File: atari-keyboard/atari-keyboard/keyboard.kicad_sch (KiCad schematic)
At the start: 210 parts, among them SW201 MENU, SW202 TURBO, SW203 RESET, SW204 OPTION, SW205 SELECT, SW206 START, SW207 HELP, SW208 ESC, SW209 RSHIFT, SW210 1, SW211 2, SW212 3, SW213 4, SW214 5, SW215 6, SW216 7, SW217 8, SW218 UP, SW219 9, SW220 0, SW221 <, SW222 >, SW223 BS, SW224 BRK, SW225 TAB, SW226 Q, SW227 DOWN, SW228 W, SW229 E, SW230 R, SW231 T, SW232 Y, SW233 U, SW234 I, SW235 O, SW236 LEFT, SW237 P, SW238 [-], SW239 [=], SW240 RET, SW241 CTRL, SW242 A, SW243 S, SW244 D, SW245 RIGHT, SW246 F, SW247 G, SW248 H, SW249 J, SW250 K, SW251 L, SW252 [;], SW253 [+], SW254 N, SW255 MULT, SW256 CAPS, SW257 LSHIFT, SW258 Z, SW259 X, SW260 C, SW261 V, SW262 B, SW263 M, SW264 FN, SW265 INV, SW266 SPC, SW267 [,], SW268 [.], SW269 [/], SW270 POWER

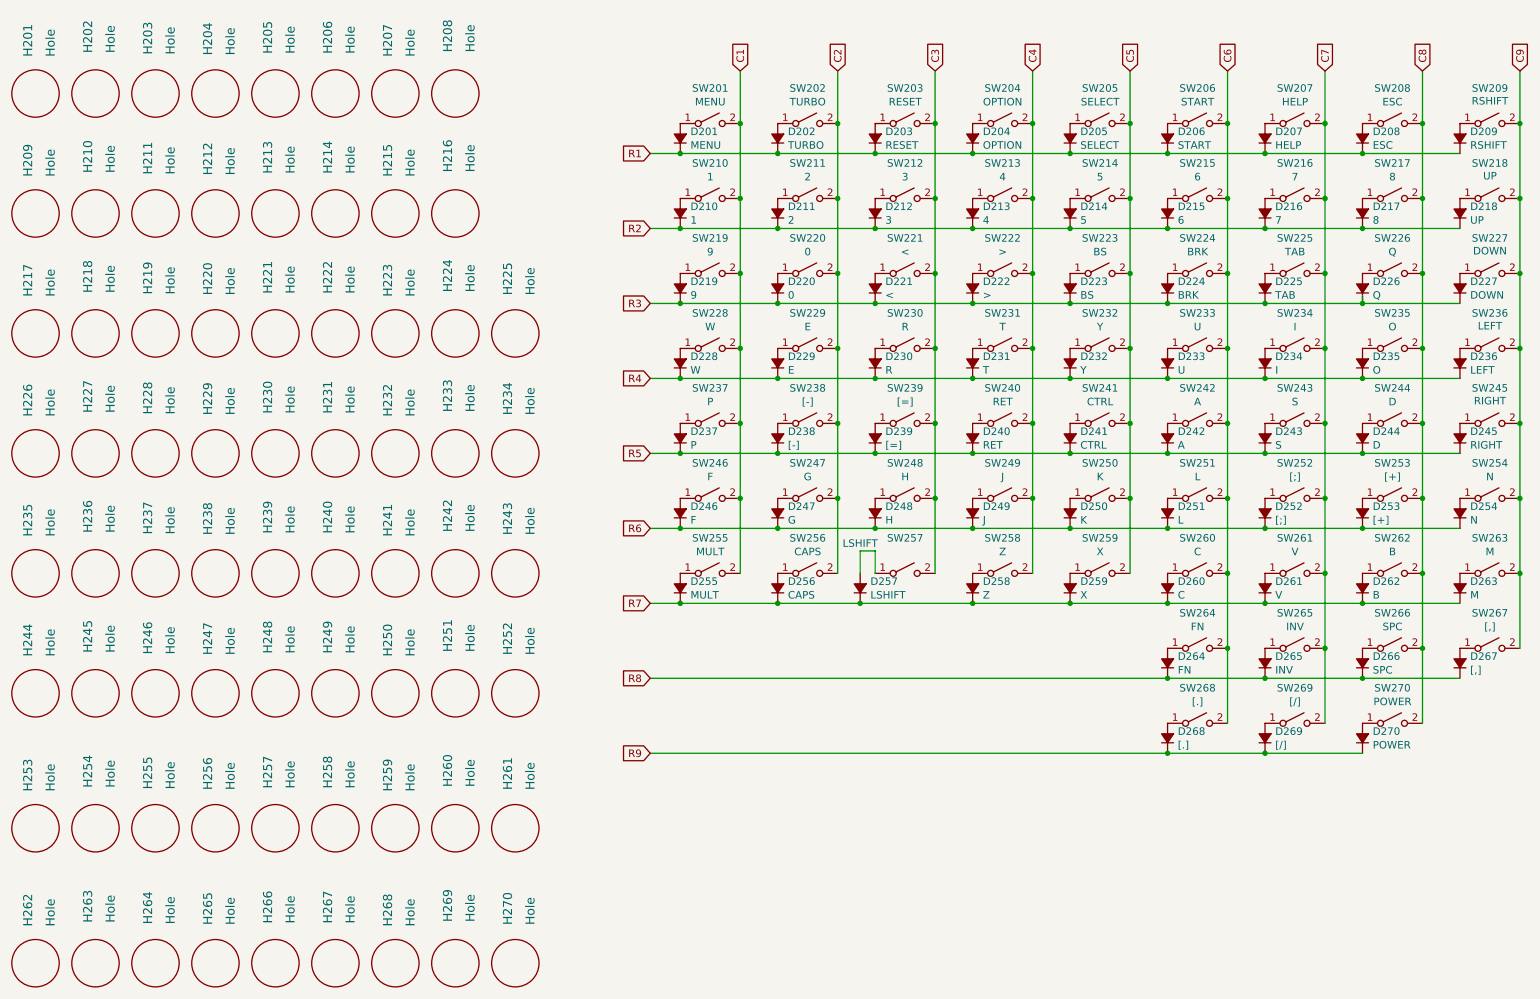
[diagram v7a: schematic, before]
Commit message: Better autogen openscad layout.  generated jlc bom&cpl
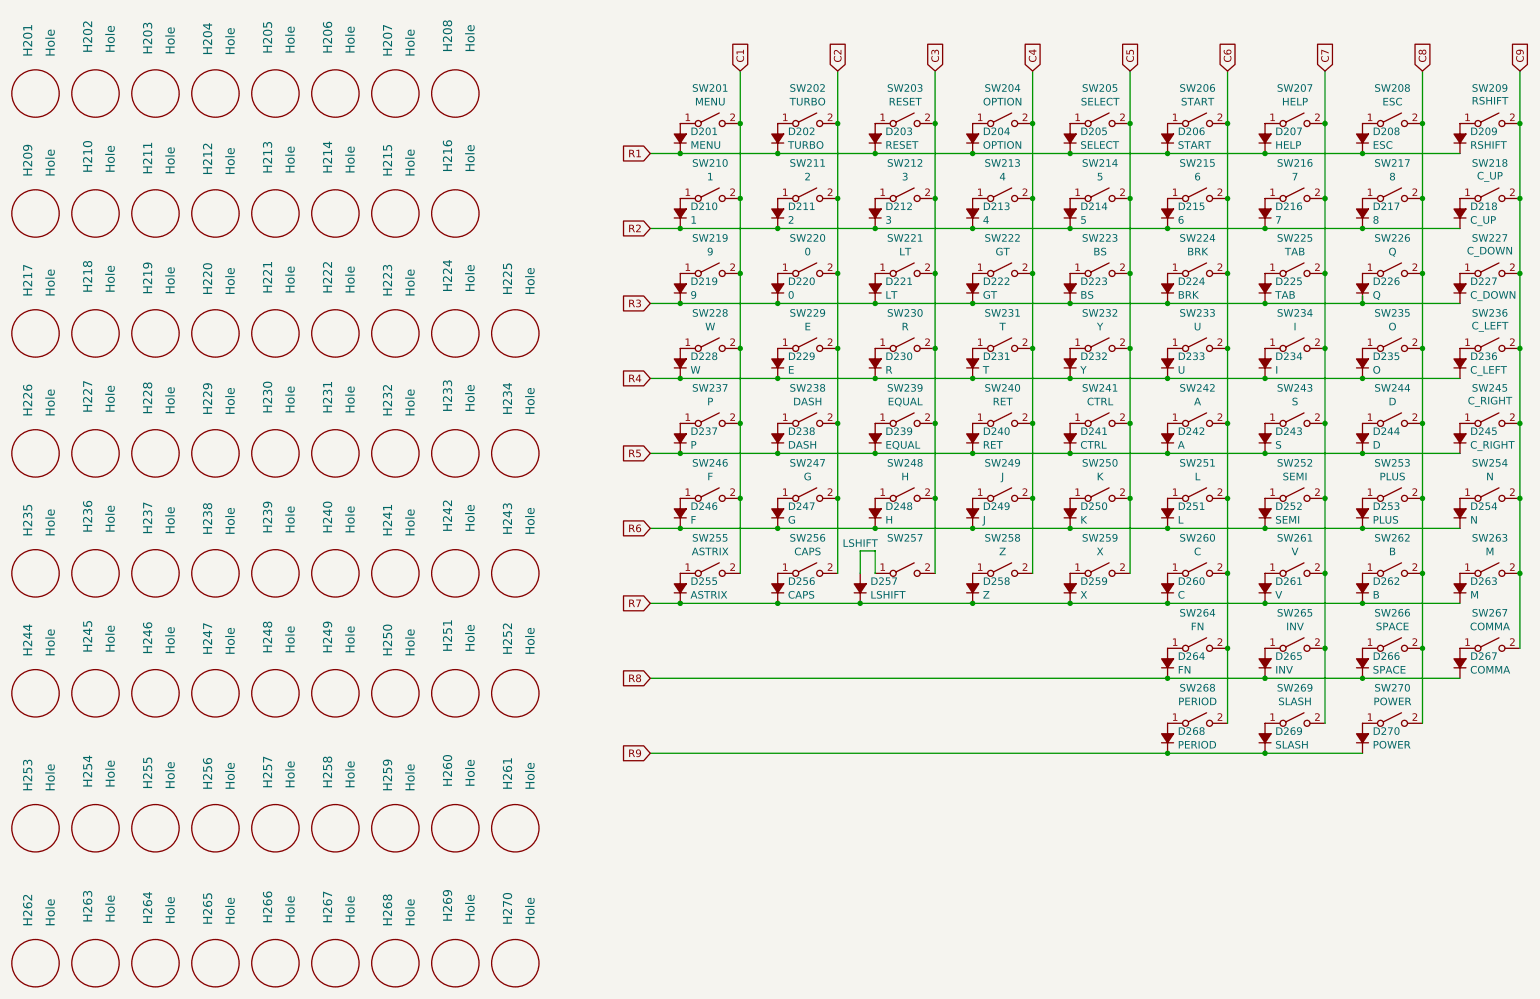
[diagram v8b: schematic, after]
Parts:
- D218, SW218: value UP -> C_UP
- D221, SW221: value < -> LT
- D222, SW222: value > -> GT
- D227, SW227: value DOWN -> C_DOWN
- D236, SW236: value LEFT -> C_LEFT
- D238, SW238: value [-] -> DASH
- D239, SW239: value [=] -> EQUAL
- D245, SW245: value RIGHT -> C_RIGHT
- D252, SW252: value [;] -> SEMI
- D253, SW253: value [+] -> PLUS
- D255, SW255: value MULT -> ASTRIX
- D266, SW266: value SPC -> SPACE
- D267, SW267: value [,] -> COMMA
- D268, SW268: value [.] -> PERIOD
- D269, SW269: value [/] -> SLASH
- H240: PCB_X 2 -> 4
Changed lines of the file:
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@@
       (effects (font (size 1.27 1.27)) (justify right))
     )
-    (property "Value" "[;]" (id 1) (at 237.9472 110.363 90)
+    (property "Value" "SEMI" (id 1) (at 237.9472 110.363 90)
       (effects (font (size 1.27 1.27)) (justify right))
     )
@@
     (in_bom yes) (on_board yes)
     (property "Reference" "SW253" (id 0) (at 257.81 100.711 0))
-    (property "Value" "[+]" (id 1) (at 257.81 103.0224 0))
+    (property "Value" "PLUS" (id 1) (at 257.81 103.0224 0))
     (property "Footprint" "Button_Switch_Keyboard:SW_Cherry_MX_1.00u_PCB" (id 2) (at 257.81 106.68 0)
       (effects (font (size 1.27 1.27)) hide)
@@
     (in_bom yes) (on_board yes)
     (property "Reference" "SW266" (id 0) (at 257.81 126.111 0))
-    (property "Value" "SPC" (id 1) (at 257.81 128.4224 0))
+    (property "Value" "SPACE" (id 1) (at 257.81 128.4224 0))
     (property "Footprint" "Button_Switch_Keyboard:SW_Cherry_MX_6.25u_PCB" (id 2) (at 257.81 132.08 0)
       (effects (font (size 1.27 1.27)) hide)
@@
     (in_bom yes) (on_board yes)
     (property "Reference" "SW238" (id 0) (at 158.75 88.011 0))
-    (property "Value" "[-]" (id 1) (at 158.75 90.3224 0))
+    (property "Value" "DASH" (id 1) (at 158.75 90.3224 0))
     (property "Footprint" "Button_Switch_Keyboard:SW_Cherry_MX_1.00u_PCB" (id 2) (at 158.75 93.98 0)
       (effects (font (size 1.27 1.27)) hide)
@@
       (effects (font (size 1.27 1.27)) (justify right))
     )
-    (property "Value" "RIGHT" (id 1) (at 270.9672 97.663 90)
+    (property "Value" "C_RIGHT" (id 1) (at 270.9672 97.663 90)
       (effects (font (size 1.27 1.27)) (justify right))
     )
@@
       (effects (font (size 1.27 1.27)) (justify right))
     )
-    (property "Value" "[/]" (id 1) (at 237.9472 148.463 90)
+    (property "Value" "SLASH" (id 1) (at 237.9472 148.463 90)
       (effects (font (size 1.27 1.27)) (justify right))
     )
@@
       (effects (font (size 1.27 1.27)) (justify right))
     )
-    (property "Value" "[=]" (id 1) (at 171.9072 97.663 90)
+    (property "Value" "EQUAL" (id 1) (at 171.9072 97.663 90)
       (effects (font (size 1.27 1.27)) (justify right))
     )
@@
       (effects (font (size 1.27 1.27)) (justify right))
     )
-    (property "Value" "MULT" (id 1) (at 138.8872 123.063 90)
+    (property "Value" "ASTRIX" (id 1) (at 138.8872 123.063 90)
       (effects (font (size 1.27 1.27)) (justify right))
     )
@@
       (effects (font (size 1.27 1.27)) (justify right))
     )
-    (property "Value" "[,]" (id 1) (at 270.9672 135.763 90)
+    (property "Value" "COMMA" (id 1) (at 270.9672 135.763 90)
       (effects (font (size 1.27 1.27)) (justify right))
     )
@@
     (in_bom yes) (on_board yes)
     (property "Reference" "SW227" (id 0) (at 274.32 62.611 0))
-    (property "Value" "DOWN" (id 1) (at 274.32 64.77 0))
+    (property "Value" "C_DOWN" (id 1) (at 274.32 64.77 0))
     (property "Footprint" "Button_Switch_Keyboard:SW_Cherry_MX_1.00u_PCB" (id 2) (at 274.32 68.58 0)
       (effects (font (size 1.27 1.27)) hide)
@@
     (in_bom yes) (on_board yes)
     (property "Reference" "SW218" (id 0) (at 274.32 49.911 0))
-    (property "Value" "UP" (id 1) (at 274.32 52.07 0))
+    (property "Value" "C_UP" (id 1) (at 274.32 52.07 0))
     (property "Footprint" "Button_Switch_Keyboard:SW_Cherry_MX_1.00u_PCB" (id 2) (at 274.32 55.88 0)
       (effects (font (size 1.27 1.27)) hide)
@@
       (effects (font (size 1.27 1.27)) (justify right))
     )
-    (property "Value" "SPC" (id 1) (at 254.4572 135.763 90)
+    (property "Value" "SPACE" (id 1) (at 254.4572 135.763 90)
       (effects (font (size 1.27 1.27)) (justify right))
     )
@@
       (effects (font (size 1.27 1.27)) (justify right))
     )
-    (property "Value" "[.]" (id 1) (at 221.4372 148.463 90)
+    (property "Value" "PERIOD" (id 1) (at 221.4372 148.463 90)
       (effects (font (size 1.27 1.27)) (justify right))
     )
@@
       (effects (font (size 1.27 1.27)) (justify right))
     )
-    (property "Value" "DOWN" (id 1) (at 270.9672 72.263 90)
+    (property "Value" "C_DOWN" (id 1) (at 270.9672 72.263 90)
       (effects (font (size 1.27 1.27)) (justify right))
     )
@@
     (in_bom yes) (on_board yes)
     (property "Reference" "SW236" (id 0) (at 274.32 75.311 0))
-    (property "Value" "LEFT" (id 1) (at 274.32 77.47 0))
+    (property "Value" "C_LEFT" (id 1) (at 274.32 77.47 0))
     (property "Footprint" "Button_Switch_Keyboard:SW_Cherry_MX_1.00u_PCB" (id 2) (at 274.32 81.28 0)
       (effects (font (size 1.27 1.27)) hide)
@@
       (effects (font (size 1.27 1.27)) (justify right))
     )
-    (property "Value" "UP" (id 1) (at 270.9672 59.563 90)
+    (property "Value" "C_UP" (id 1) (at 270.9672 59.563 90)
       (effects (font (size 1.27 1.27)) (justify right))
     )
@@
       (effects (font (size 1.27 1.27)) (justify right))
     )
-    (property "Value" "[+]" (id 1) (at 254.4572 110.363 90)
+    (property "Value" "PLUS" (id 1) (at 254.4572 110.363 90)
       (effects (font (size 1.27 1.27)) (justify right))
     )
@@
     (in_bom yes) (on_board yes)
     (property "Reference" "SW268" (id 0) (at 224.79 138.811 0))
-    (property "Value" "[.]" (id 1) (at 224.79 141.1224 0))
+    (property "Value" "PERIOD" (id 1) (at 224.79 141.1224 0))
     (property "Footprint" "Button_Switch_Keyboard:SW_Cherry_MX_1.00u_PCB" (id 2) (at 224.79 144.78 0)
       (effects (font (size 1.27 1.27)) hide)
@@
       (effects (font (size 1.27 1.27)) (justify right))
     )
-    (property "Value" "<" (id 1) (at 171.9072 72.263 90)
+    (property "Value" "LT" (id 1) (at 171.9072 72.263 90)
       (effects (font (size 1.27 1.27)) (justify right))
     )
@@
     (in_bom yes) (on_board yes)
     (property "Reference" "SW239" (id 0) (at 175.26 88.011 0))
-    (property "Value" "[=]" (id 1) (at 175.26 90.3224 0))
+    (property "Value" "EQUAL" (id 1) (at 175.26 90.3224 0))
     (property "Footprint" "Button_Switch_Keyboard:SW_Cherry_MX_1.00u_PCB" (id 2) (at 175.26 93.98 0)
       (effects (font (size 1.27 1.27)) hide)
@@
     (in_bom yes) (on_board yes)
     (property "Reference" "SW221" (id 0) (at 175.26 62.611 0))
-    (property "Value" "<" (id 1) (at 175.26 64.9224 0))
+    (property "Value" "LT" (id 1) (at 175.26 64.9224 0))
     (property "Footprint" "Button_Switch_Keyboard:SW_Cherry_MX_1.00u_PCB" (id 2) (at 175.26 68.58 0)
       (effects (font (size 1.27 1.27)) hide)
@@
     (in_bom yes) (on_board yes)
     (property "Reference" "SW255" (id 0) (at 142.24 113.411 0))
-    (property "Value" "MULT" (id 1) (at 142.24 115.7224 0))
+    (property "Value" "ASTRIX" (id 1) (at 142.24 115.7224 0))
     (property "Footprint" "Button_Switch_Keyboard:SW_Cherry_MX_1.00u_PCB" (id 2) (at 142.24 119.38 0)
       (effects (font (size 1.27 1.27)) hide)
@@
     (in_bom yes) (on_board yes)
     (property "Reference" "SW269" (id 0) (at 241.3 138.811 0))
-    (property "Value" "[/]" (id 1) (at 241.3 141.1224 0))
+    (property "Value" "SLASH" (id 1) (at 241.3 141.1224 0))
     (property "Footprint" "Button_Switch_Keyboard:SW_Cherry_MX_1.00u_PCB" (id 2) (at 241.3 144.78 0)
       (effects (font (size 1.27 1.27)) hide)
@@
     (in_bom yes) (on_board yes)
     (property "Reference" "SW222" (id 0) (at 191.77 62.611 0))
-    (property "Value" ">" (id 1) (at 191.77 64.9224 0))
+    (property "Value" "GT" (id 1) (at 191.77 64.9224 0))
     (property "Footprint" "Button_Switch_Keyboard:SW_Cherry_MX_1.00u_PCB" (id 2) (at 191.77 68.58 0)
       (effects (font (size 1.27 1.27)) hide)
@@
     (in_bom yes) (on_board yes)
     (property "Reference" "SW245" (id 0) (at 274.32 88.011 0))
-    (property "Value" "RIGHT" (id 1) (at 274.32 90.17 0))
+    (property "Value" "C_RIGHT" (id 1) (at 274.32 90.17 0))
     (property "Footprint" "Button_Switch_Keyboard:SW_Cherry_MX_1.00u_PCB" (id 2) (at 274.32 93.98 0)
       (effects (font (size 1.27 1.27)) hide)
@@
     (in_bom yes) (on_board yes)
     (property "Reference" "SW252" (id 0) (at 241.3 100.711 0))
-    (property "Value" "[;]" (id 1) (at 241.3 103.0224 0))
+    (property "Value" "SEMI" (id 1) (at 241.3 103.0224 0))
     (property "Footprint" "Button_Switch_Keyboard:SW_Cherry_MX_1.00u_PCB" (id 2) (at 241.3 106.68 0)
       (effects (font (size 1.27 1.27)) hide)
@@
       (effects (font (size 1.27 1.27)) (justify right))
     )
-    (property "Value" "LEFT" (id 1) (at 270.9672 84.963 90)
+    (property "Value" "C_LEFT" (id 1) (at 270.9672 84.963 90)
       (effects (font (size 1.27 1.27)) (justify right))
     )
@@
     (in_bom yes) (on_board yes)
     (property "Reference" "SW267" (id 0) (at 274.32 126.111 0))
-    (property "Value" "[,]" (id 1) (at 274.32 128.4224 0))
+    (property "Value" "COMMA" (id 1) (at 274.32 128.4224 0))
     (property "Footprint" "Button_Switch_Keyboard:SW_Cherry_MX_1.00u_PCB" (id 2) (at 274.32 132.08 0)
       (effects (font (size 1.27 1.27)) hide)
@@
       (effects (font (size 1.27 1.27)) (justify right))
     )
-    (property "Value" "[-]" (id 1) (at 155.3972 97.663 90)
+    (property "Value" "DASH" (id 1) (at 155.3972 97.663 90)
       (effects (font (size 1.27 1.27)) (justify right))
     )
@@
       (effects (font (size 1.524 1.524)) hide)
     )
-    (property "PCB_X" "2" (id 4) (at 78.74 119.38 0)
+    (property "PCB_X" "4" (id 4) (at 78.74 119.38 0)
       (effects (font (size 1.27 1.27)) hide)
     )
@@
       (effects (font (size 1.27 1.27)) (justify right))
     )
-    (property "Value" ">" (id 1) (at 188.4172 72.263 90)
-      (effects (font (size 1.27 1.27)) (justify right))
-    )
+    (property "Value" "GT" (id 1) (at 188.4172 72.263 90)
+      (effects (font (size 1.27 1.27)) (justify right))
+    )
